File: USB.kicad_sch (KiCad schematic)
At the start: 16 parts, among them J401 USB_B_Micro, Q401 S8050, Q402 S8050, U401 CH340C

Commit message: Changed to ESP32-S3-WROOM-1U
Added ESP32-S3-WROOM-1U-N16R2  and updated all routing and pin assignments.

Added USB-OTG connected via JST-PH
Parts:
- added J402: Conn_01x04, Connector_JST:JST_SH_BM04B-SRSS-TB_1x04-1MP_P1.00mm_Vertical, symbol Connector_Generic:Conn_01x04
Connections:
- new net USB_D_MINUS: J402.2 (Pin_2)
- new net USB_D_PLUS: J402.3 (Pin_3)
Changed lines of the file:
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@@
+	(wire
+		(pts
+			(xy 210.82 100.33) (xy 214.63 100.33)
+		)
+		(stroke
+			(width 0)
+			(type default)
+		)
+	)
 	(wire
 		(pts
@@
 		(pts
 			(xy 52.07 95.25) (xy 52.07 111.76)
+		)
+		(stroke
+			(width 0)
+			(type default)
+		)
+	)
+	(wire
+		(pts
+			(xy 210.82 97.79) (xy 214.63 97.79)
 		)
 		(stroke
@@
 				(hide yes)
 			)
+		)
+	)
+	(hierarchical_label "USB_D_PLUS"
+		(shape bidirectional)
+		(at 210.82 100.33 180)
+		(effects
+			(font
+				(size 1.27 1.27)
+			)
+			(justify right)
+		)
+	)
+	(hierarchical_label "USB_D_MINUS"
+		(shape bidirectional)
+		(at 210.82 97.79 180)
+		(effects
+			(font
+				(size 1.27 1.27)
+			)
+			(justify right)
 		)
 	)
@@
 					(unit 1)
 				)
+			)
+		)
+	)
+	(symbol
+		(lib_id "Connector_Generic:Conn_01x04")
+		(at 219.71 97.79 0)
+		(unit 1)
+		(exclude_from_sim no)
+		(in_bom yes)
+		(on_board yes)
+		(dnp no)
+		(fields_autoplaced yes)
+		(property "Reference" "J402"
+			(at 222.25 97.7899 0)
+			(effects
+				(font
+					(size 1.27 1.27)
+				)
+				(justify left)
+			)
+		)
+		(property "Value" "Conn_01x04"
+			(at 222.25 100.3299 0)
+			(effects
+				(font
+					(size 1.27 1.27)
+				)
+				(justify left)
+			)
+		)
+		(property "Footprint" "Connector_JST:JST_SH_BM04B-SRSS-TB_1x04-1MP_P1.00mm_Vertical"
+			(at 219.71 97.79 0)
+			(effects
+				(font
+					(size 1.27 1.27)
+				)
+				(hide yes)
+			)
+		)
+		(property "Datasheet" "~"
+			(at 219.71 97.79 0)
+			(effects
+				(font
+					(size 1.27 1.27)
+				)
+				(hide yes)
+			)
+		)
+		(property "Description" "Generic connector, single row, 01x04, script generated (kicad-library-utils/schlib/autogen/connector/)"
+			(at 219.71 97.79 0)
+			(effects
+				(font
+					(size 1.27 1.27)
+				)
+				(hide yes)
+			)
+		)
+		(pin "3"
+		)
+		(pin "4"
+		)
+		(pin "1"
+		)
+		(pin "2"
+		)
+		(instances
+			(project ""
+				(path "/dff502f1-2fe5-4c09-a767-aabc78c2e052/00000000-0000-0000-0000-00005f89c30a"
+					(reference "J402")
+					(unit 1)
+				)

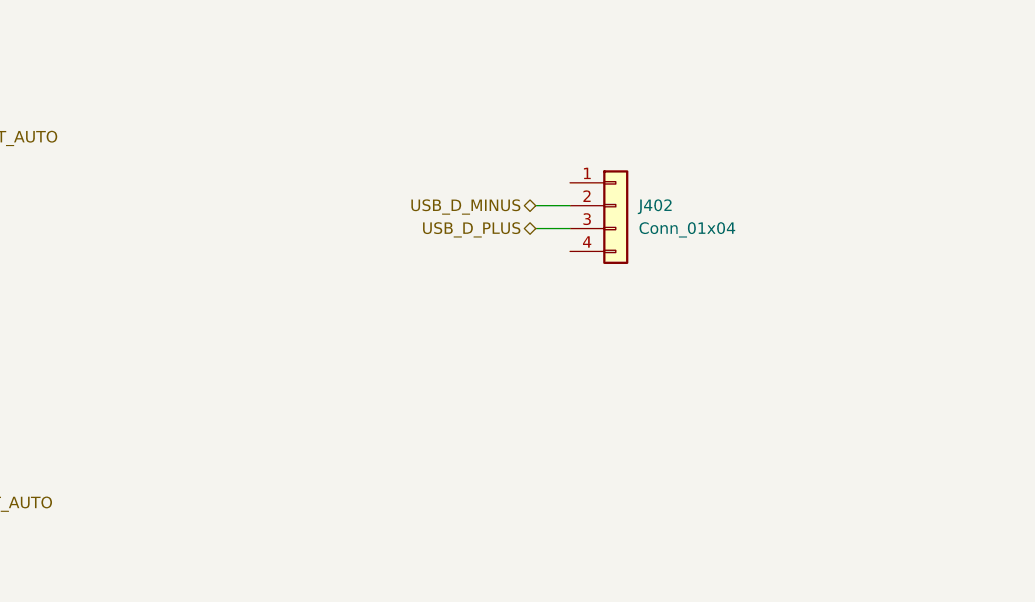
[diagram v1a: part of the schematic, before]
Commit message: Added TSV/ESD to the native USB
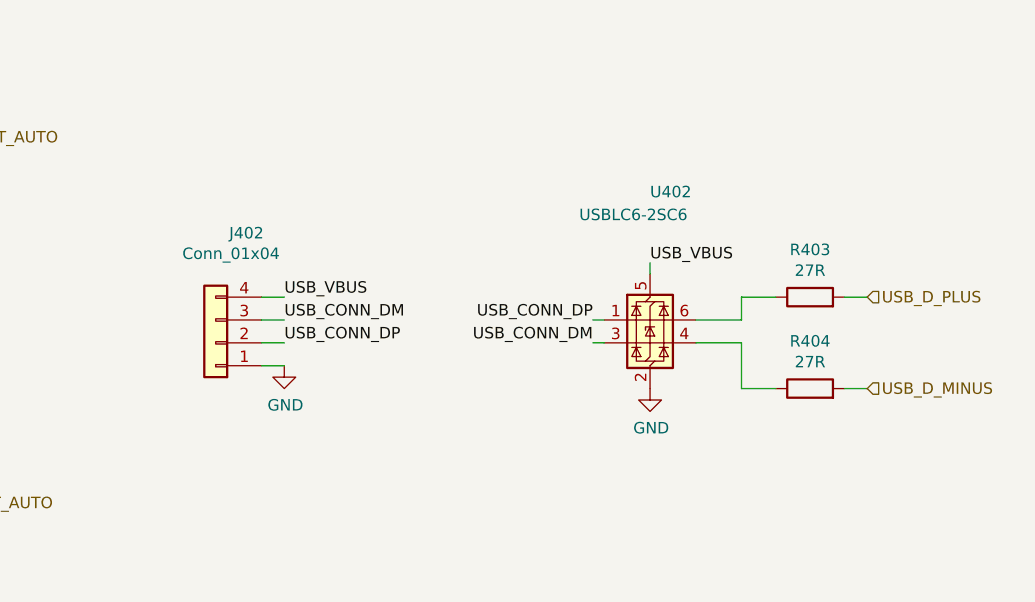
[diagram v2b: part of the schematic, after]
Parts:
- added R403, R404: 27R, Resistor_SMD:R_0201_0603Metric, symbol Device:R
- added U402: USBLC6-2SC6, Package_TO_SOT_SMD:SOT-23-6, symbol Power_Protection:USBLC6-2SC6
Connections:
- net GND: now also J402.1 (Pin_1), U402.2 (GND)
- net USB_D_MINUS: now also R404.2; no longer J402.2 (Pin_2)
- net USB_D_PLUS: now also R403.2; no longer J402.3 (Pin_3)
- net USB_VBUS: now reaches J402.4 (Pin_4)
- net USB_VBUS: now also U402.5 (VBUS)
- new net: R404.1, U402.4 (I/O2)
- new net: R403.1, U402.6 (I/O1)
- new net USB_CONN_DM: J402.3 (Pin_3), U402.3 (I/O2)
- new net USB_CONN_DP: J402.2 (Pin_2), U402.1 (I/O1)
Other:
- moved on the sheet: J402

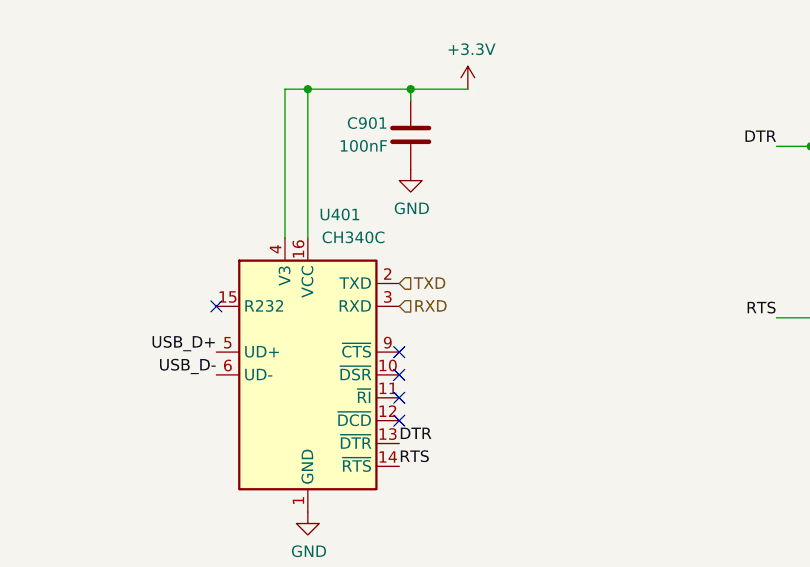
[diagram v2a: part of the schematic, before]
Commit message: Net renaming and Silkscreen tidy ups
The UART / Serial naming convention is revised for more consistency
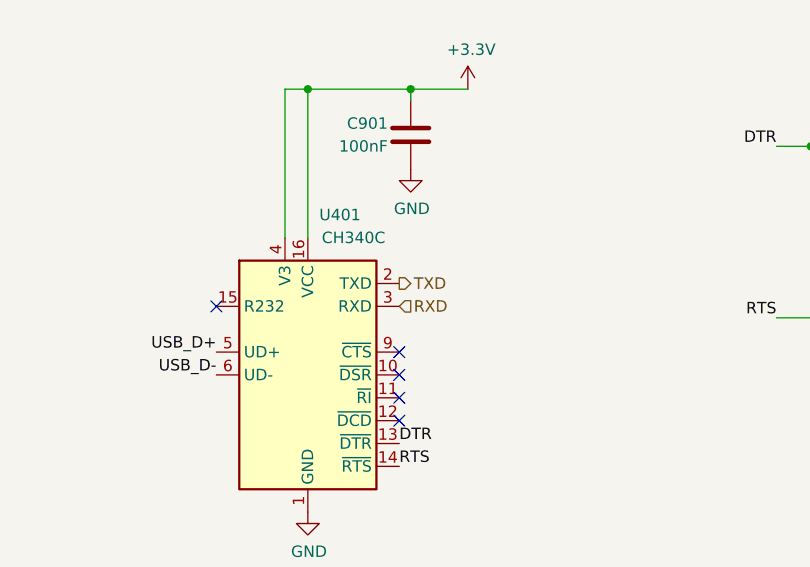
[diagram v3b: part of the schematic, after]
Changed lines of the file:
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@@
 	)
 	(hierarchical_label "TXD"
-		(shape input)
+		(shape output)
 		(at 62.23 116.84 0)
 		(effects

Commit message: Updated LCSC part numbers
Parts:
- J402: LCSC (none) -> C160390
- U402: LCSC (none) -> C7519
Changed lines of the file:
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@@
+			)
+		)
+		(property "LCSC" "C160390"
+			(at 175.26 113.03 0)
+			(effects
+				(font
+					(size 1.27 1.27)
+				)
+				(hide yes)
 			)
 		)
@@
 			(at 223.52 110.49 0)
 			(effects
+				(font
+					(size 1.27 1.27)
+				)
+				(hide yes)
+			)
+		)
+		(property "LCSC" "C7519"
+			(at 223.52 110.49 0)
+			(effects

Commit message: Moved ESP32-S3 + larger pin headers
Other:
- company: Hat Labs Ltd -> Fifty One North Limited
- title: Hat Labs Marine Engine & Tank interface (HALMET) -> Bluefin Marine Processor
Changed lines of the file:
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@@
 	(paper "A4")
 	(title_block
-		(title "Hat Labs Marine Engine & Tank interface (HALMET)")
-		(date "2024-01-18")
-		(rev "1.0.1")
-		(company "Hat Labs Ltd")
-		(comment 1 "https://creativecommons.org/licenses/by-sa/4.0")
-		(comment 2 "To view a copy of this license, visit ")
-		(comment 3 "HALMET is licensed under CC BY-SA 4.0.")
+		(title "Bluefin Marine Processor")
+		(date "2026-01-08")
+		(rev "1.0.0")
+		(company "Fifty One North Limited")
+		(comment 1 "https://creativecommons.org/licenses/by-sa/4.0/")
+		(comment 2 "Bluefin is licensed under CC BY-SA 4.0")
+		(comment 3 "Modifications © 2026 Fiftyone North Ltd.")
+		(comment 4 "Based on an original design by Hat Labs Ltd.")
 	)
 	(text "C403 and C404 are virtual for now"
